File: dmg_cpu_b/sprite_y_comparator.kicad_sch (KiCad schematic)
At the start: 119 parts

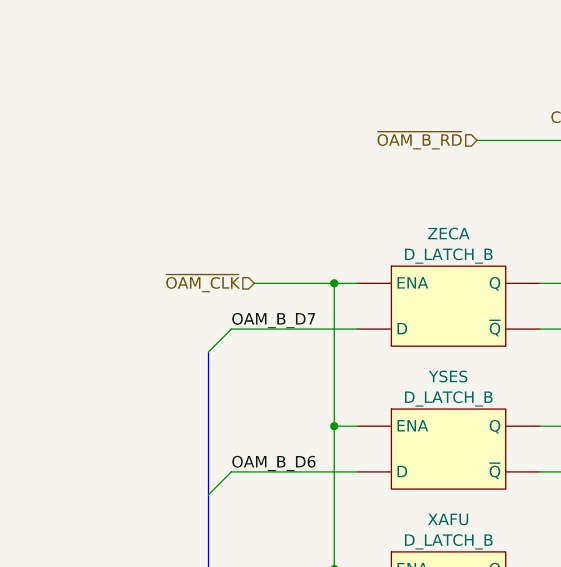
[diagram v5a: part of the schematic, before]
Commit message: Changes made based on review. PPU hierarchcal sheet work started.
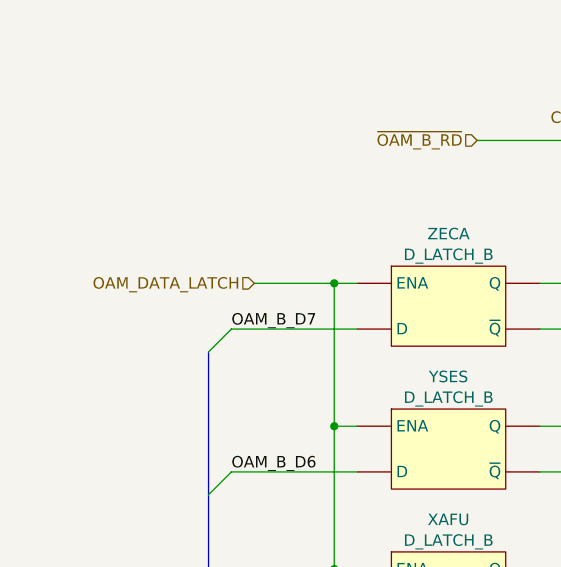
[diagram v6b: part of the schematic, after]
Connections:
- net ~{OAM_CLK} renamed OAM_DATA_LATCH
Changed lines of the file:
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@@
     (effects (font (size 1.27 1.27)) (justify right))
   )
-  (hierarchical_label "~{OAM_CLK}" (shape input) (at 37.465 53.975 180)
+  (hierarchical_label "OAM_DATA_LATCH" (shape input) (at 37.465 53.975 180)
     (effects (font (size 1.27 1.27)) (justify right))
   )

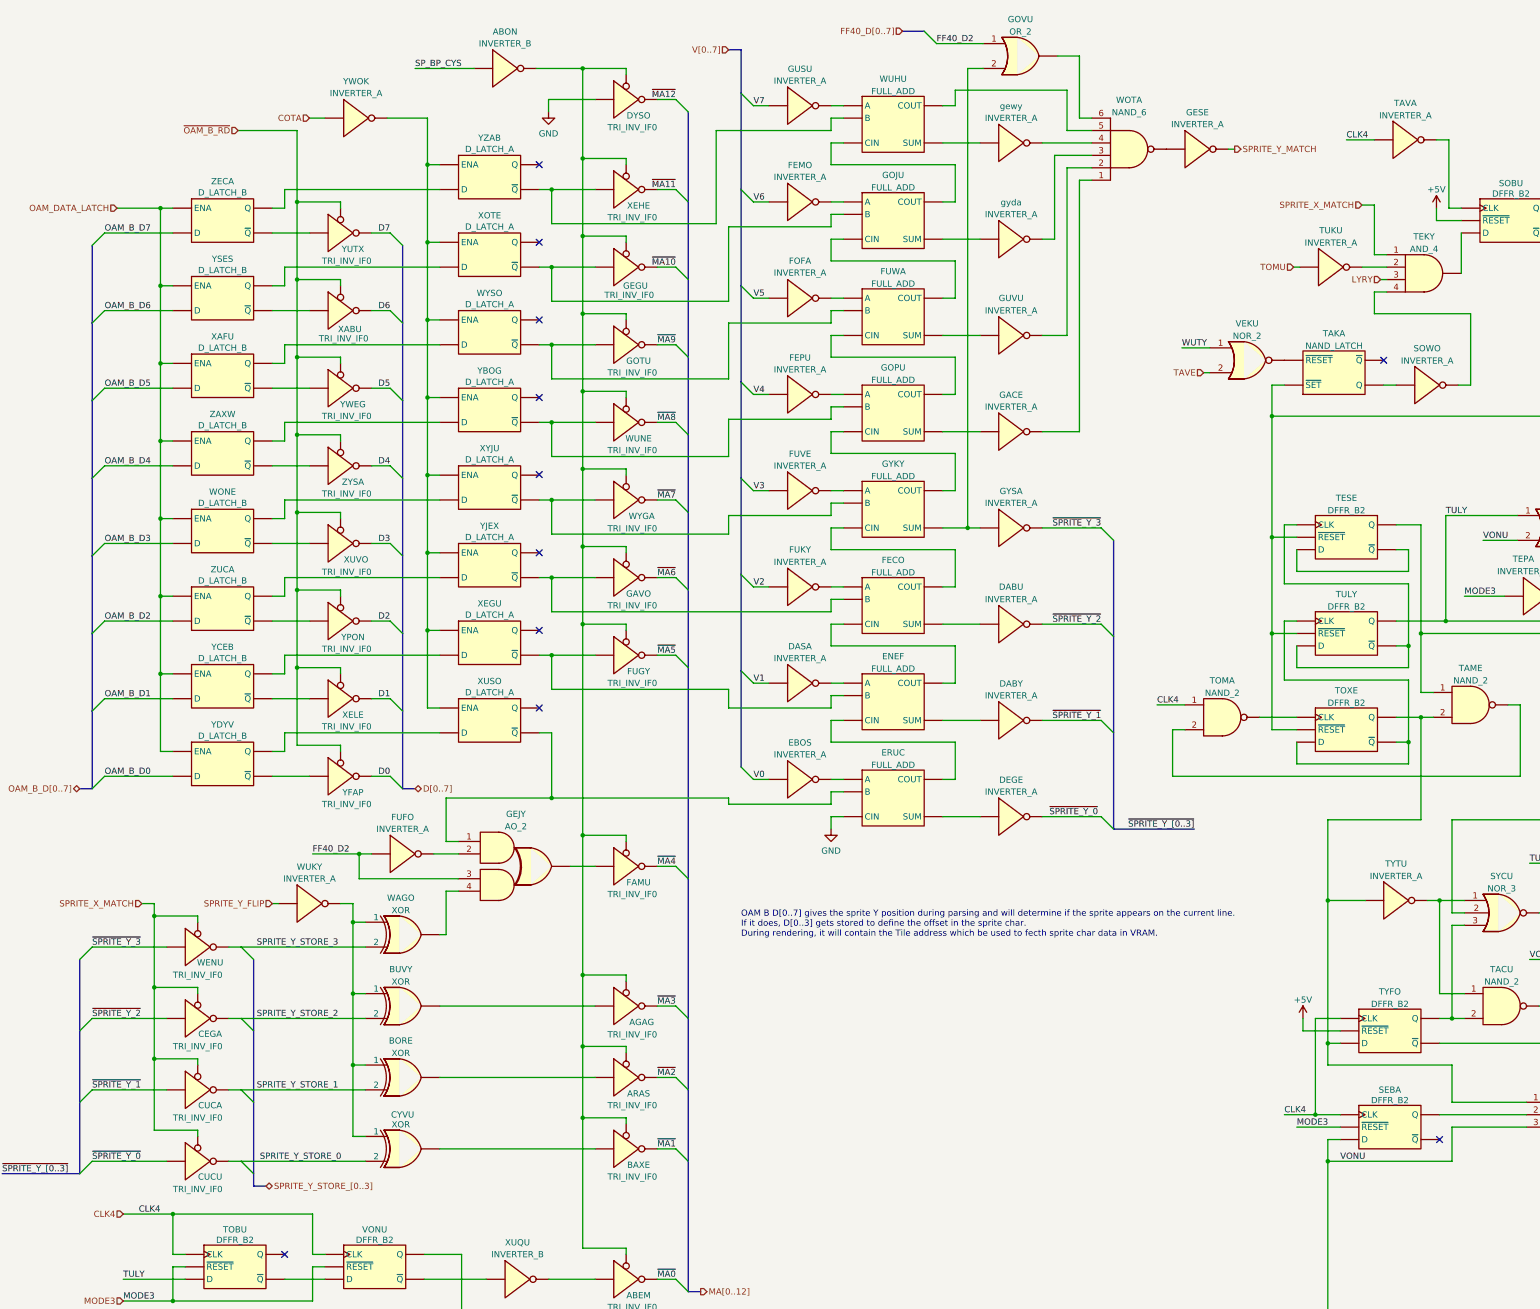
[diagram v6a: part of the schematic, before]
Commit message: PPU hierarchical page progress. Elements moved out of window sheet to be includes in BG and WIN cycles sheet
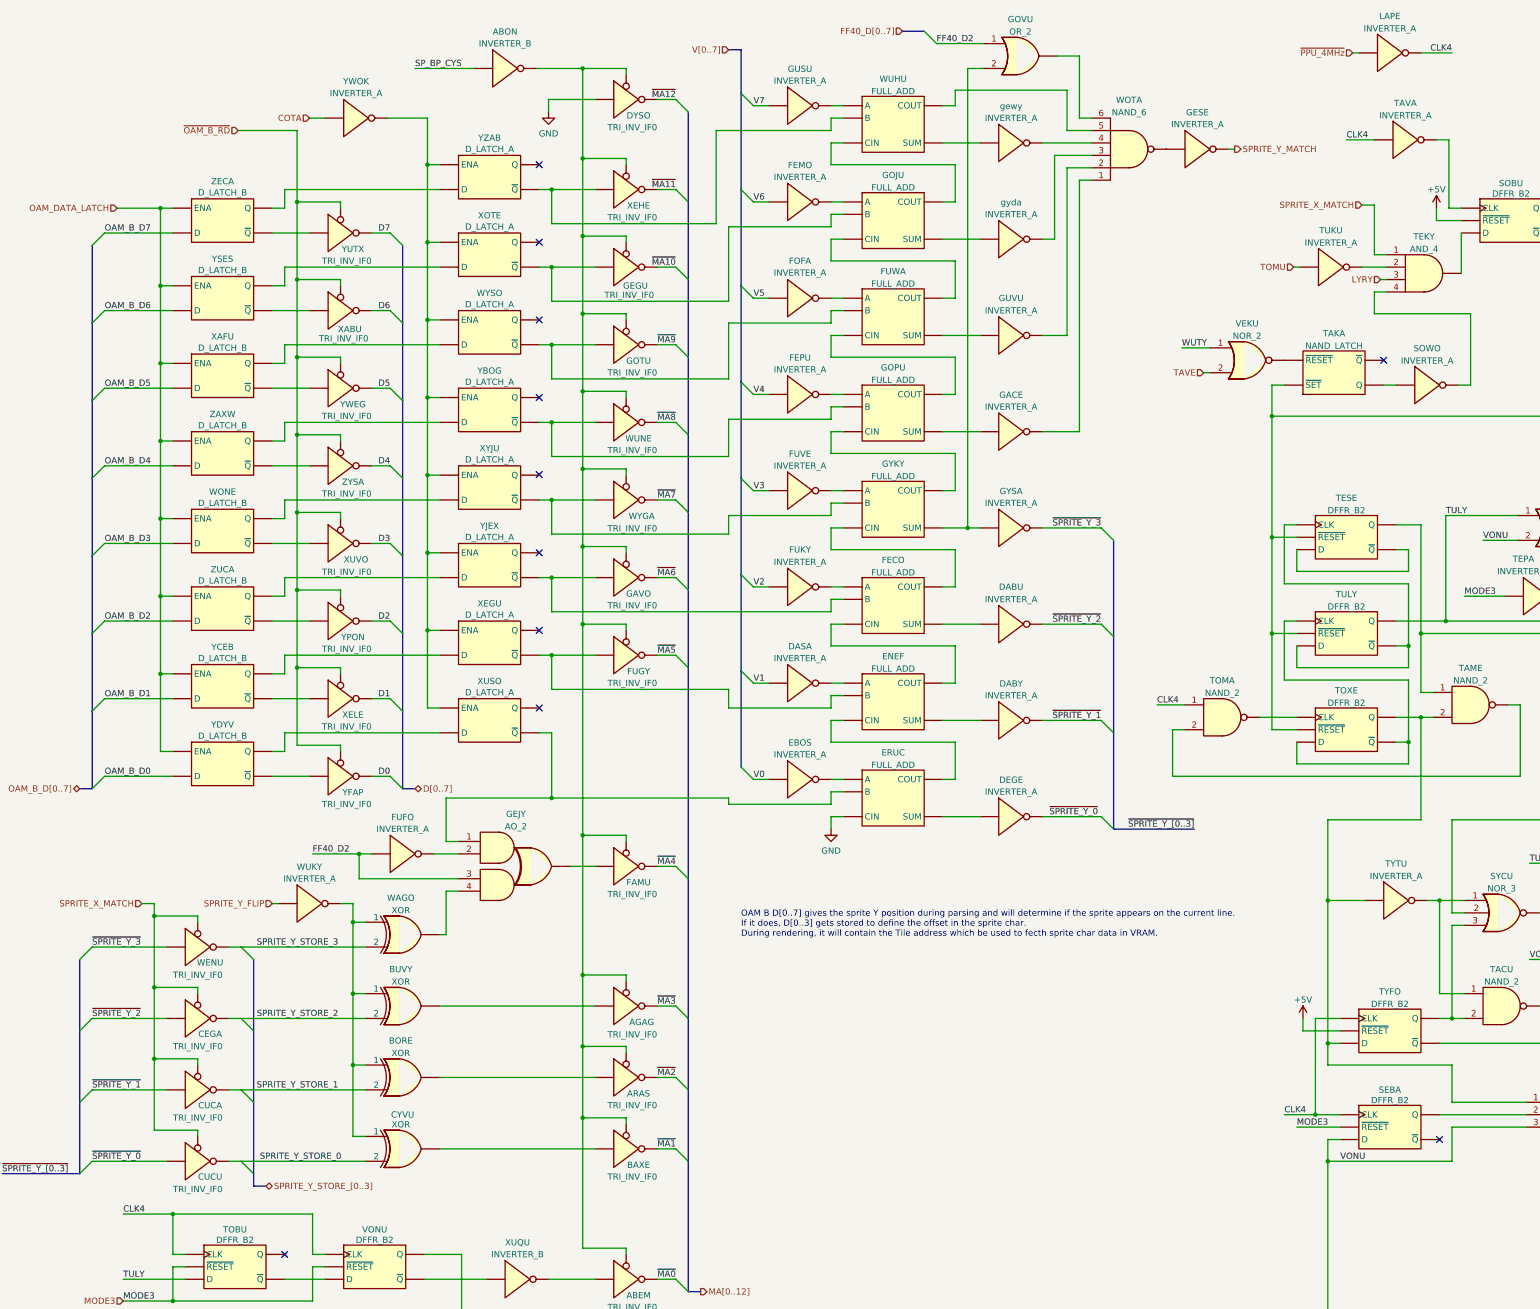
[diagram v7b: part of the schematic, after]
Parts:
- added LAPE: INVERTER_A, symbol DMG_CPU_Cells:INVERTER_A
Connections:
- net CLK4: now also LAPE.2
- new net ~{PPU_4MHz}: LAPE.1
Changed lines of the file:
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@@
+    (stroke (width 0) (type default) (color 0 0 0 0))
+  )
+  (wire (pts (xy 291.465 22.225) (xy 290.195 22.225))
     (stroke (width 0) (type default) (color 0 0 0 0))
   )
@@
   )
   (wire (pts (xy 167.64 52.705) (xy 170.815 52.705))
+    (stroke (width 0) (type default) (color 0 0 0 0))
+  )
+  (wire (pts (xy 304.165 22.225) (xy 310.515 22.225))
     (stroke (width 0) (type default) (color 0 0 0 0))
   )
@@
     (effects (font (size 1.27 1.27)) (justify right bottom))
   )
+  (label "CLK4" (at 310.515 22.225 180)
+    (effects (font (size 1.27 1.27)) (justify right bottom))
+  )
   (label "TULY" (at 326.39 187.96 0)
     (effects (font (size 1.27 1.27)) (justify left bottom))
@@
     (effects (font (size 1.27 1.27)) (justify left bottom))
   )
-  (label "CLK4" (at 41.91 259.715 0)
+  (label "CLK4" (at 38.735 259.715 0)
     (effects (font (size 1.27 1.27)) (justify left bottom))
   )
@@
     (effects (font (size 1.27 1.27)) (justify right))
   )
+  (hierarchical_label "~{PPU_4MHz}" (shape input) (at 290.195 22.225 180)
+    (effects (font (size 1.27 1.27)) (justify right))
+  )
   (hierarchical_label "MODE3" (shape input) (at 38.735 277.495 180)
     (effects (font (size 1.27 1.27)) (justify right))
@@
   (hierarchical_label "SPRITE_Y_STORE_[0..3]" (shape tri_state) (at 67.945 254 0)
     (effects (font (size 1.27 1.27)) (justify left))
-  )
-  (hierarchical_label "CLK4" (shape input) (at 38.735 259.715 180)
-    (effects (font (size 1.27 1.27)) (justify right))
   )
   (hierarchical_label "OAM_B_D[0..7]" (shape bidirectional) (at 29.845 172.72 180)
@@
     (pin "5")
   )
+  (symbol (lib_id "DMG_CPU_Cells:INVERTER_A") (at 297.815 22.225 0) (unit 1)
+    (in_bom yes) (on_board yes) (fields_autoplaced)
+    (property "Reference" "LAPE" (id 0) (at 297.815 14.7152 0))
+    (property "Value" "INVERTER_A" (id 1) (at 297.815 17.2521 0))
+    (property "Footprint" "" (id 2) (at 295.275 22.225 0)
+      (effects (font (size 1.27 1.27)) hide)
+    )
+    (property "Datasheet" "http://iceboy.a-singer.de/doc/dmg_cells.html#inv_a" (id 3) (at 299.085 29.845 0)
+      (effects (font (size 1.27 1.27)) hide)
+    )
+    (pin "1")
+    (pin "2")
+  )
   (symbol (lib_id "DMG_CPU_Cells:TRI_INV_IF0") (at 83.185 170.18 0) (unit 1)
